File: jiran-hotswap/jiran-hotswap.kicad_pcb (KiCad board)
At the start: 2 copper layers, 152.3 x 104.7 mm, 132 parts, among them J1 TRRS, Q1 2N7002, SW1 SW_Push, SW10 SW_Push, SW11 SW_Push, SW12 SW_Push, SW13 SW_Push, SW14 SW_Push, SW15 SW_Push, SW16 SW_Push, SW17 SW_Push, SW18 SW_Push, SW19 SW_Push, SW2 SW_Push, SW20 SW_Push, SW21 SW_Push, SW22 SW_Push, SW23 SW_Push, SW24 SW_Push, SW25 SW_Push, SW26 SW_Push, SW27 SW_Push, SW28 SW_Push, SW29 SW_Push, SW3 SW_Push, SW4 SW_Push, SW5 SW_Push, SW6 SW_Push, SW7 SW_Push, SW8 SW_Push, SW9 SW_Push, U1 ProMicro

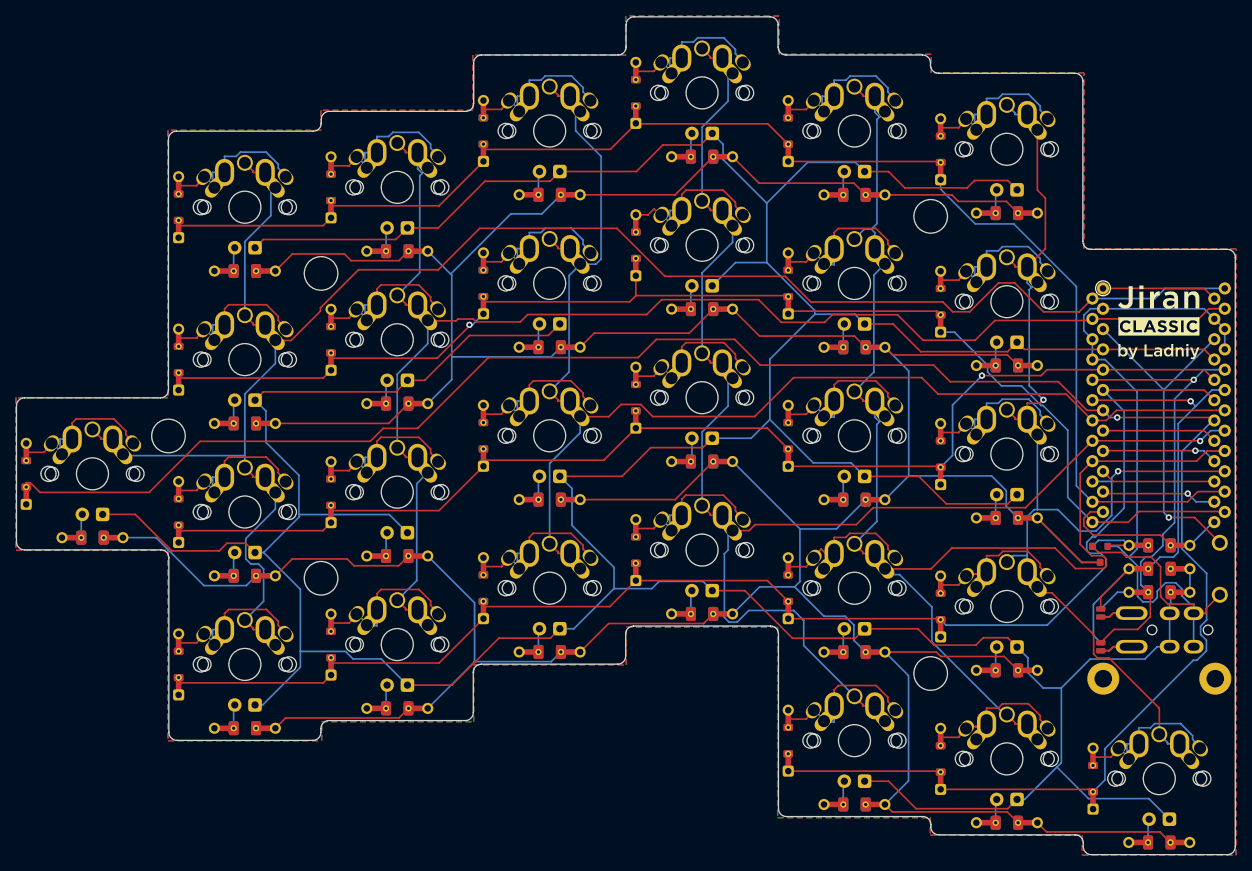
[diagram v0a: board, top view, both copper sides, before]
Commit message: Update logo, change switch footprints, move diode footprints
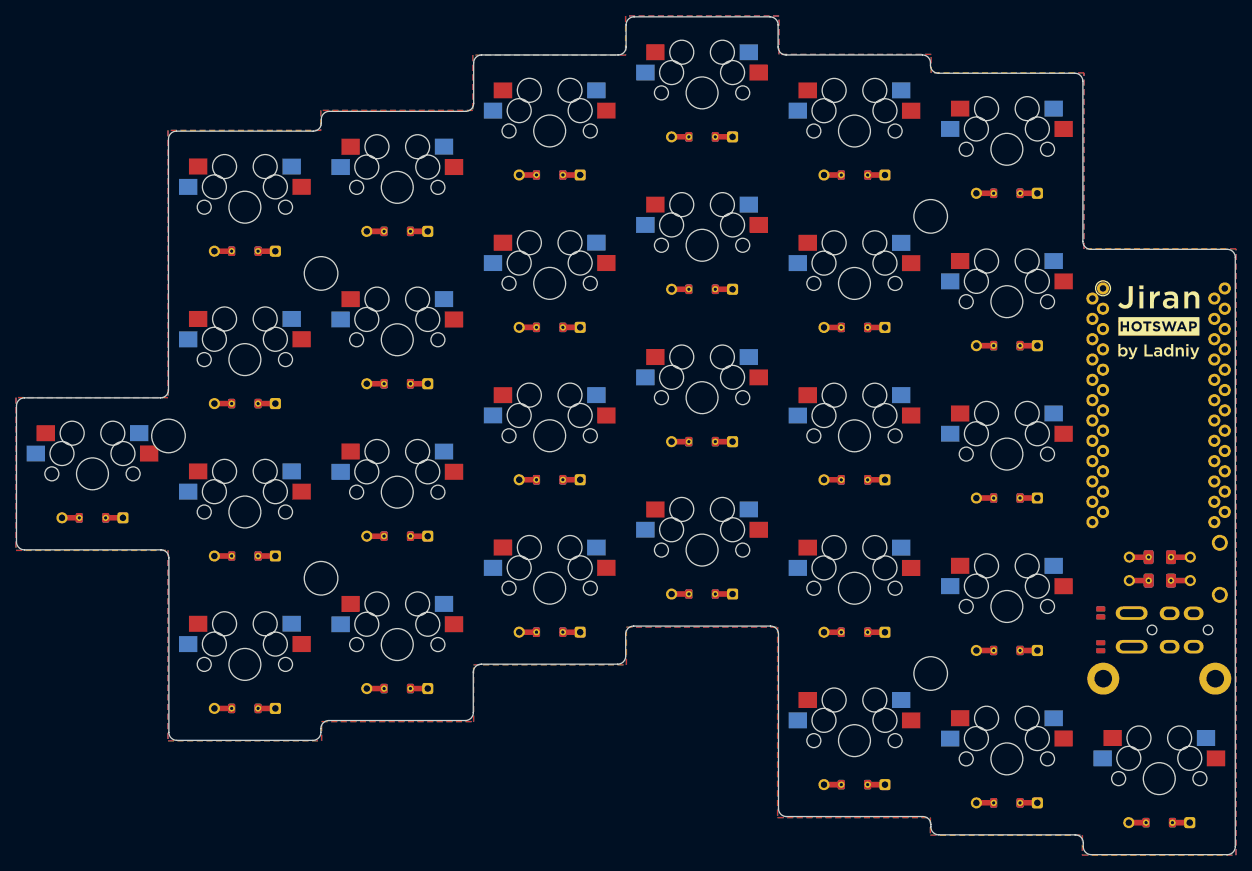
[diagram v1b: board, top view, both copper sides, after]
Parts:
- removed D29, D30, D31, D32, D33, D34, D35, D36, D37, D38, D39, D40, D41, D42, D43, D44, D45, D46, D47, D48, D49, D50, D51, D52, D53, D54, D55, D56: LED_Small, used_footprints:LED_THT
- removed Q1: 2N7002, used_footprints:Mosfet_SMD_Dual_SOT-23
- removed R1, R10, R11, R12, R13, R14, R15, R16, R17, R18, R19, R2, R20, R21, R22, R23, R24, R25, R26, R27, R28, R3, R4, R5, R6, R7, R8, R9: 300R, used_footprints:Resistor_Hybrid_1205
- removed R31: 100k, used_footprints:Resistor_Hybrid_1205
- G1, G2: value LOGO -> logo-jiran-hotswap; footprint used_footprints:Silk_Logotype -> used_footprints:Silk_Logo_Hotswap
- SW1, SW10, SW11, SW12, SW13, SW14, SW15, SW16, SW17, SW18, SW19, SW2, SW20, SW21, SW22, SW23, SW24, SW25, SW26, SW27, SW28, SW3, SW4, SW5, SW6, SW7, SW8, SW9: footprint used_footprints:Switch_MxAlpsChoc_MillMax_1u -> used_footprints:Switch_Mx_Hotswap_1u
- moved D27 9.94 mm to (201.0, 128.4), turned to 180 degrees
- moved D28 9.94 mm to (220.0, 130.8), turned to 180 degrees
- moved D11 9.94 mm to (181.9, 68.9), turned to 180 degrees
- moved D10 9.94 mm to (162.9, 64.2), turned to 180 degrees
- moved D12 9.94 mm to (201.0, 71.2), turned to 180 degrees
- moved D14 9.94 mm to (124.8, 95.0), turned to 180 degrees
- moved D15 9.94 mm to (143.8, 88.0), turned to 180 degrees
- moved D16 9.94 mm to (162.9, 83.2), turned to 180 degrees
- moved D17 9.94 mm to (181.9, 88.0), turned to 180 degrees
- moved D18 9.94 mm to (201.0, 90.3), turned to 180 degrees
- moved D2 9.94 mm to (124.8, 56.9), turned to 180 degrees
- moved D20 9.94 mm to (124.8, 114.1), turned to 180 degrees
- moved D21 9.94 mm to (143.8, 107.0), turned to 180 degrees
- moved D22 9.94 mm to (162.9, 102.3), turned to 180 degrees
- moved D23 9.94 mm to (181.9, 107.0), turned to 180 degrees
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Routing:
- net VCC: track 606.9 -> 0.00 mm
- net /LEDOut: track 579.6 -> 0.00 mm
- net /rowE: track 264.9 -> 0.00 mm, vias 1 -> 0
- net /col0: track 231.6 -> 0.00 mm
- net /col3: track 182.8 -> 0.00 mm, vias 1 -> 0
- net /rowA: track 181.4 -> 0.00 mm
- net /col1: track 180.6 -> 0.00 mm
- net /rowD: track 178.9 -> 0.00 mm
- net /col4: track 169.3 -> 0.00 mm
- net /col2: track 167.0 -> 0.00 mm
- net /rowB: track 165.4 -> 0.00 mm, vias 1 -> 0
- net /rowC: track 157.2 -> 0.00 mm, vias 1 -> 0
- net /col5: track 143.2 -> 0.00 mm, vias 2 -> 0
- net GND: track 103.7 -> 0.00 mm
- net SDA: track 64.7 -> 0.00 mm, vias 1 -> 0
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
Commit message: Fill all zones
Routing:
- net /col0: track 0.00 -> 308.6 mm, vias 0 -> 1
- net /col3: track 0.00 -> 247.8 mm, vias 0 -> 3
- net /col4: track 0.00 -> 245.9 mm, vias 0 -> 4
- net /col2: track 0.00 -> 245.2 mm, vias 0 -> 3
- net /rowE: track 0.00 -> 239.4 mm
- net /col1: track 0.00 -> 231.1 mm, vias 0 -> 2
- net /col5: track 0.00 -> 214.9 mm, vias 0 -> 4
- net /rowA: track 0.00 -> 169.9 mm
- net /rowB: track 0.00 -> 159.1 mm
- net /rowD: track 0.00 -> 157.3 mm, vias 0 -> 1
- net /rowC: track 0.00 -> 145.9 mm
- net GND: track 0.00 -> 69.5 mm
- net SDA: track 0.00 -> 63.7 mm, vias 0 -> 1
- net SCL: track 0.00 -> 60.8 mm, vias 0 -> 1
- net VCC: track 0.00 -> 60.2 mm
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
